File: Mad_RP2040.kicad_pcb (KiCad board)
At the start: 4 copper layers, 80 x 106.8 mm, 119 parts, among them J1 USB_C_Receptacle, Q1 2N7002PV,115, SW1 SW_SPST, SW10 SW_SPST, SW100 EVPAA202K, SW11 SW_SPST, SW12 SW_SPST, SW13 SW_SPST, SW14 SW_SPST, SW15 SW_SPST, SW16 SW_SPST, SW17 SW_SPST, SW18 SW_SPST, SW19 SW_SPST, SW2 SW_SPST, SW20 SW_SPST, SW3 SW_SPST, SW4 SW_SPST, SW5 SW_SPST, SW6 SW_SPST, SW7 SW_SPST, SW8 SW_SPST, SW9 SW_SPST, U2 ECMF02-2AMX6, U3 NCP1117-3.3, U4 W25Q128JVSIQ, U5 RP2040, X1 ECS-2520MVLC-120-CN

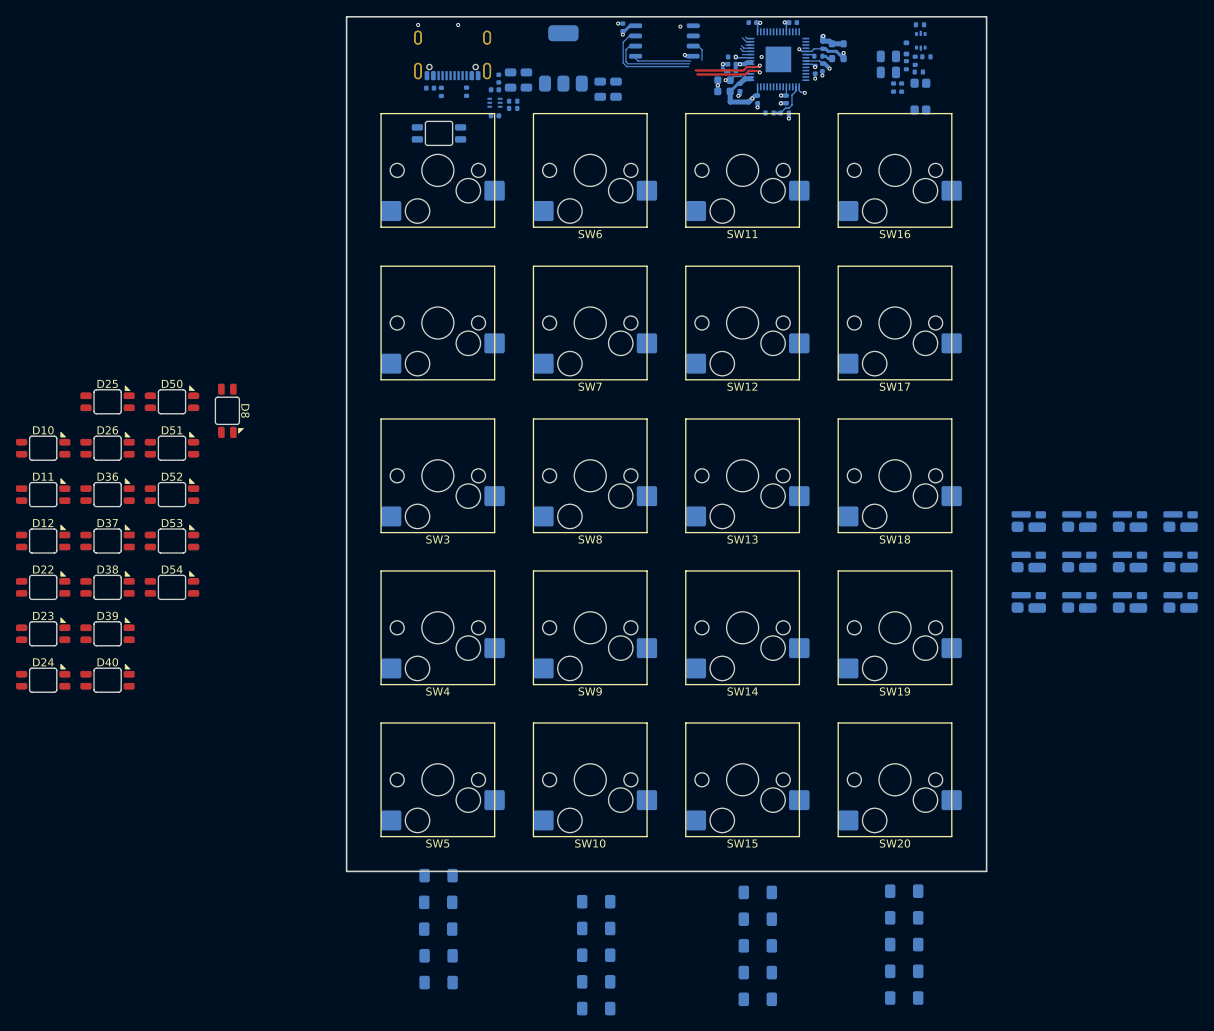
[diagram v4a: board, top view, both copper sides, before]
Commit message: Rough placement of components. Remove one layer of keys (4x4 -> 4x3)
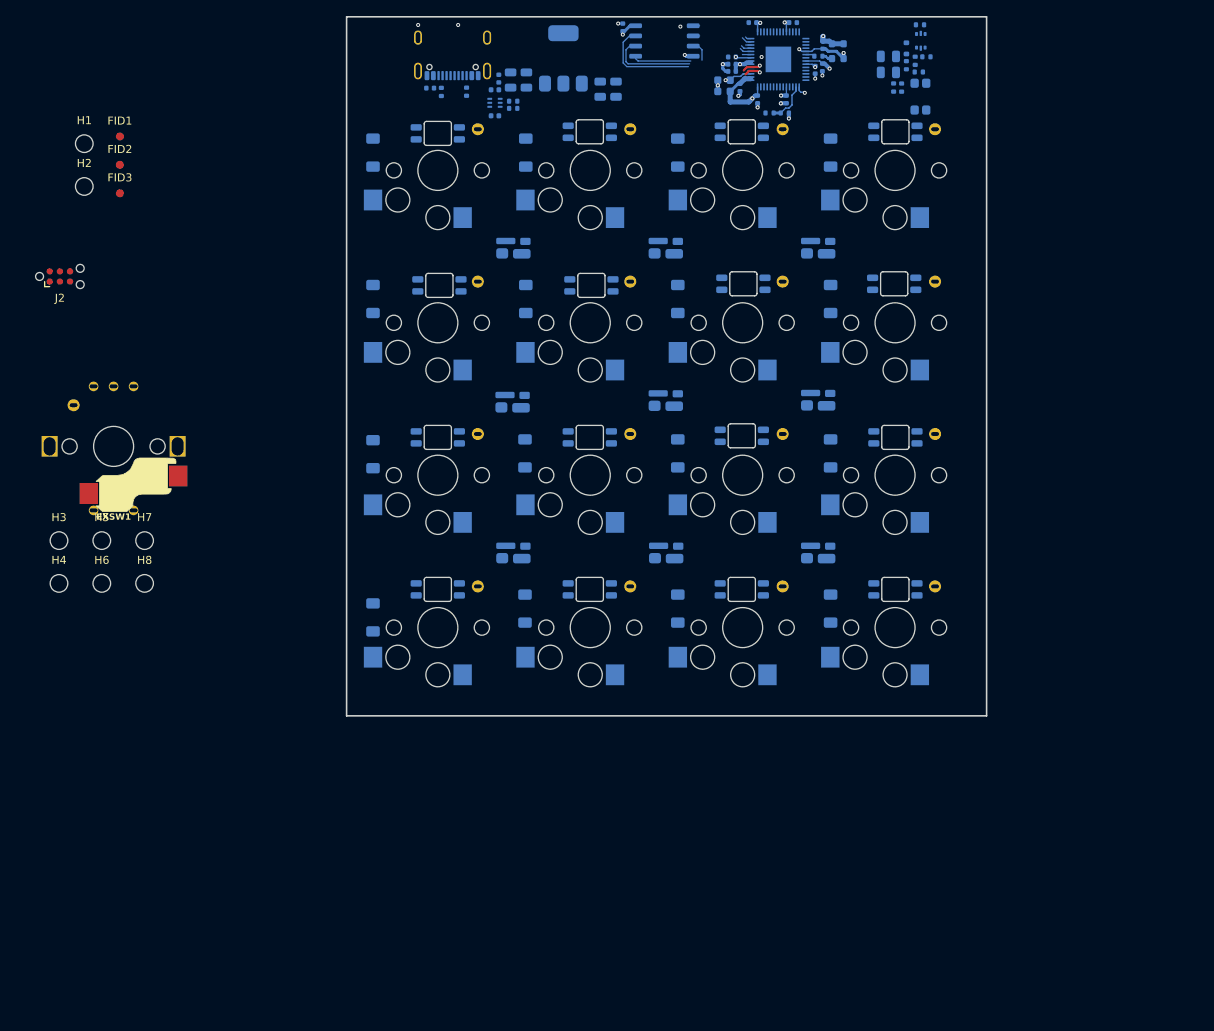
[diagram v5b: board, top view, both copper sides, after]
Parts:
- removed D12, D26, D40, D54: SK6812_MINI_E, Mad_Footprints:SK6812MINI-E
- removed D16, D30, D44: SK6812MINI, Mad_Footprints:SK6812MINI-012
- removed D21, D35, D49, D5: LL4148, Diode_SMD:D_MiniMELF
- removed SW10, SW15, SW20, SW5: SW_SPST, Mad_Footprints:SW_Hotswap_Kailh_MX_1.00u
- added EXSW1: RotaryEncoder_Switch, kbd:keyswitch_choc12_hotswap_1u_rotary_encoder_ec12, F.Cu at (91.4, 96.1)
- added FID1: Fiducial, Fiducial:Fiducial_1mm_Mask2mm, F.Cu at (92.2, 57.4)
- added FID2: Fiducial, Fiducial:Fiducial_1mm_Mask2mm, F.Cu at (92.2, 60.9)
- added FID3: Fiducial, Fiducial:Fiducial_1mm_Mask2mm, F.Cu at (92.2, 64.5)
- added H1: MountingHole_Pad, MountingHole:MountingHole_2.2mm_M2_DIN965, F.Cu at (87.8, 58.3)
- added H2: MountingHole_Pad, MountingHole:MountingHole_2.2mm_M2_DIN965, F.Cu at (87.8, 63.6)
- added H3: MountingHole_Pad, MountingHole:MountingHole_2.2mm_M2_DIN965, F.Cu at (84.6, 107.9)
- added H4: MountingHole_Pad, MountingHole:MountingHole_2.2mm_M2_DIN965, F.Cu at (84.6, 113.2)
- added H5: MountingHole_Pad, MountingHole:MountingHole_2.2mm_M2_DIN965, F.Cu at (90.0, 107.9)
- added H6: MountingHole_Pad, MountingHole:MountingHole_2.2mm_M2_DIN965, F.Cu at (90.0, 113.2)
- added H7: MountingHole_Pad, MountingHole:MountingHole_2.2mm_M2_DIN965, F.Cu at (95.3, 107.9)
- added H8: MountingHole_Pad, MountingHole:MountingHole_2.2mm_M2_DIN965, F.Cu at (95.3, 113.2)
- added J2: Conn_ARM_SWD_TagConnect_TC2030-NL, Connector:Tag-Connect_TC2030-IDC-NL_2x03_P1.27mm_Vertical, F.Cu at (84.7, 74.9)
- added T1: Tab, PCM_kikit:Tab, F.Cu at (84.3, 57.2)
- added T2: Tab, PCM_kikit:Tab, F.Cu at (84.3, 60.5)
- added T3: Tab, PCM_kikit:Tab, F.Cu at (84.3, 63.8)
- added T4: Tab, PCM_kikit:Tab, F.Cu at (84.3, 67.1)
- added U1: PCB, Mad_Footprints:BOM, F.Cu at (92.6, 68.0)
- D10, D11, D22, D23, D24, D25, D36, D37, D38, D39, D50, D51, D52, D53, D8: moved to B.Cu
- SW1, SW11, SW12, SW13, SW14, SW16, SW17, SW18, SW19, SW2, SW3, SW4, SW6, SW7, SW8, SW9: footprint Mad_Footprints:SW_Hotswap_Kailh_MX_1.00u -> kbd:keyswitch_choc12_hotswap_1u; moved to B.Cu
- moved D17 107.4 mm to (142.9, 59.4), turned to -90 degrees
- moved D31 106.3 mm to (161.9, 59.4), turned to -90 degrees
- moved D45 106.1 mm to (181.1, 59.4), turned to -90 degrees
- moved D1 104.1 mm to (123.8, 59.4), turned to -90 degrees
- moved D50 96.5 mm to (189.2, 56.8), turned to 180 degrees
- moved D51 92.6 mm to (189.0, 75.8), turned to 180 degrees
- moved D36 91.3 mm to (169.9, 56.8), turned to 180 degrees
- moved D52 90.7 mm to (189.2, 95.0), turned to 180 degrees
- moved D53 90.6 mm to (189.2, 114.0), turned to 180 degrees
- moved D22 88.9 mm to (150.9, 56.8), turned to 180 degrees
- moved D18 85.8 mm to (142.9, 77.7), turned to -90 degrees
- moved D37 85.7 mm to (170.2, 75.8), turned to 180 degrees
- moved D32 84.8 mm to (161.9, 77.7), turned to -90 degrees
- moved D46 84.5 mm to (181.1, 77.7), turned to -90 degrees
- moved D2 82.5 mm to (123.8, 77.7), turned to -90 degrees
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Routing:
- net /RP2040/RP2040/USB_D+: track 9.46 -> 3.46 mm
- net /RP2040/RP2040/USB_D-: track 9.25 -> 3.25 mm
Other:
- board size 80 x 106.8 mm -> 80 x 87.4 mm

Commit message: More placement, start routing, fix up some schematic connections
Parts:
- removed D14, D27, D28, D29, D42: SK6812MINI, Mad_Footprints:SK6812MINI-012
- removed H1, H3, H5, H7: MountingHole_Pad, MountingHole:MountingHole_2.2mm_M2_DIN965
- removed the SW1 at (132.0, 61.6)
- added C23: 100nF, Capacitor_SMD:C_0402_1005Metric, B.Cu at (138.1, 51.8)
- added D16: SK6812MINI, Mad_Footprints:SK6812MINI-012, B.Cu at (160.5, 90.2)
- added H10: MountingHole_Pad, MountingHole:MountingHole_2.2mm_M2_DIN965, F.Cu at (193.1, 46.4)
- added H11: MountingHole_Pad, MountingHole:MountingHole_2.2mm_M2_DIN965, F.Cu at (127.9, 46.4)
- H2, H4, H6, H8, J2: moved to B.Cu
- SW1: renamed from EXSW1; moved to B.Cu
- moved J2 115.9 mm to (196.9, 46.0), turned to -90 degrees
- moved H6 92.5 mm to (179.6, 90.2)
- moved H2 73.2 mm to (160.5, 71.1)
- moved H8 65.4 mm to (160.5, 109.2), turned to 180 degrees
- moved H4 61.4 mm to (141.5, 90.2)
- moved SW1 53.2 mm to (132.0, 61.6), turned to 180 degrees
- moved R9 9.51 mm to (180.4, 51.8), turned to 180 degrees
- moved R7 9.36 mm to (184.9, 49.3), turned to 90 degrees
- moved SW100 9.30 mm to (186.9, 44.8), turned to 180 degrees
- moved R15 8.63 mm to (180.4, 52.8), turned to 0 degrees
- moved C9 7.64 mm to (182.4, 52.3), turned to -90 degrees
- moved Q1 7.61 mm to (186.9, 50.8), turned to 180 degrees
- moved R6 5.00 mm to (188.9, 50.3), turned to -90 degrees
- moved C8 4.83 mm to (184.4, 52.3), turned to -90 degrees
- moved R8 4.74 mm to (185.9, 47.3), turned to 0 degrees
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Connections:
- D22 pad 2: +5V -> Net-(D22-DOUT)
- D25 pad 4: Net-(D25-DIN) -> Net-(D11-DOUT)
- D36 pad 4: +5V -> Net-(D22-DOUT)
- D41 pad 1: Net-(D27-DOUT) -> Net-(D13-DOUT)
- D43 pad 1: Net-(D29-DOUT) -> Net-(D15-DOUT)
- D43 pad 3: Net-(D16-DIN) (its old number) -> unconnected-(D43-DOUT-Pad3)
- D53 pad 4: Net-(D53-DIN) -> Net-(D39-DOUT)
- SW1 pad A: /RE0A -> /REB
- SW1 pad B: /REB -> /RE0A
- SW1 pad S1: GND -> Net-(D1-A)
- SW1 pad S2: /KEYEX1 -> /Col0
- U5 pad 12: /RP2040/IO_9 -> /Col0
- U5 pad 13: /RP2040/IO_10 -> /Col1
- U5 pad 14: /RP2040/ENC1A -> /Col2
- U5 pad 15: /RP2040/ENC1B -> /Col3
- U5 pad 16: /RP2040/ENC2A -> /RP2040/ENC1A
- U5 pad 17: /RP2040/ENC2B -> /RP2040/ENC1B
- U5 pad 18: /RP2040/ENC3A -> /RP2040/ENC2A
- U5 pad 27: /RP2040/ENC3B -> /RP2040/ENC2B
- U5 pad 8: /RP2040/IO_6 -> /Row2
- U5 pad 9: /Col0 -> /Row3
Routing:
- net +5V: track 0.00 -> 288.6 mm, vias 0 -> 16
- net /Col0: track 0.00 -> 97.2 mm
- net /Col1: track 0.00 -> 96.6 mm
- net /Col2: track 0.00 -> 90.5 mm
- net Net-(D13-DIN): track 0.00 -> 74.5 mm, vias 0 -> 2
- net /Col3: track 0.00 -> 66.7 mm
- net Net-(D16-DIN): track 0.00 -> 47.2 mm, vias 0 -> 2
- net Net-(D15-DIN): track 0.00 -> 46.9 mm, vias 0 -> 2
- net /RP2040/RP2040/QSPI_~{CS}: track 1.54 -> 41.7 mm, vias 0 -> 2
- net GND: track 16.1 -> 52.9 mm, vias 14 -> 93
- net Net-(D15-DOUT): track 0.00 -> 36.6 mm, vias 0 -> 2
- net Net-(D13-DOUT): track 0.00 -> 36.5 mm, vias 0 -> 2
- net Net-(D10-DOUT): track 0.00 -> 31.6 mm
- net /RP2040/RP2040/USB_D-: track 3.25 -> 32.2 mm, vias 1 -> 2
- net /RP2040/RP2040/USB_D+: track 3.46 -> 32.2 mm, vias 1 -> 2
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- added copper zone on B.Cu, net +5V
- added copper zone on B.Cu, net /PreFIlterGND
- added copper zone on In1.Cu, net /PreFIlterGND
- added copper zone on In2.Cu, net /PreFIlterGND
- added copper zone on In1.Cu, net /RP2040/3V3
- added copper zone on B.Cu, net GND
- added copper zone on F.Cu, net GND
- added copper zone on In1.Cu, net GND
- added copper zone on In2.Cu, net GND
- added copper zone on B.Cu, net VBUS
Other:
- board size 80 x 87.4 mm -> 77.2 x 86.4 mm

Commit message: Update tabs
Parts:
- removed FID1, FID2, FID3: Fiducial, Fiducial:Fiducial_1mm_Mask2mm
- removed U1: PCB, Mad_Footprints:BOM
- moved T1 119.5 mm to (199.2, 90.3), turned to 180 degrees
- moved T4 98.1 mm to (160.4, 129.0), turned to 90 degrees
- moved T2 73.0 mm to (154.9, 42.0), turned to -90 degrees
- moved T3 45.6 mm to (121.4, 90.3)

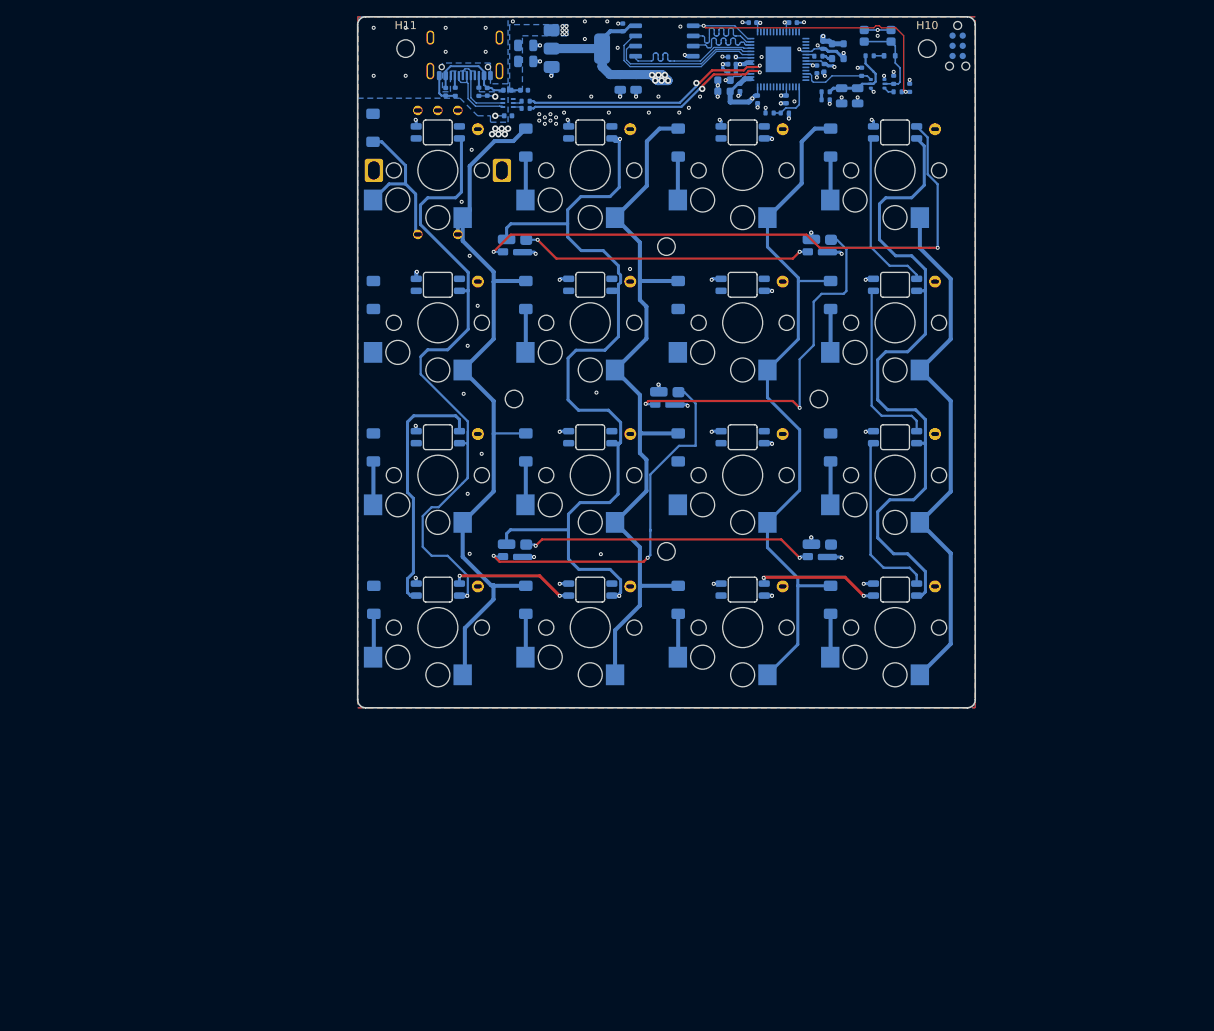
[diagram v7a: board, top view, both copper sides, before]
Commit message: Review Schematic, Add TRS connector. Continue routing
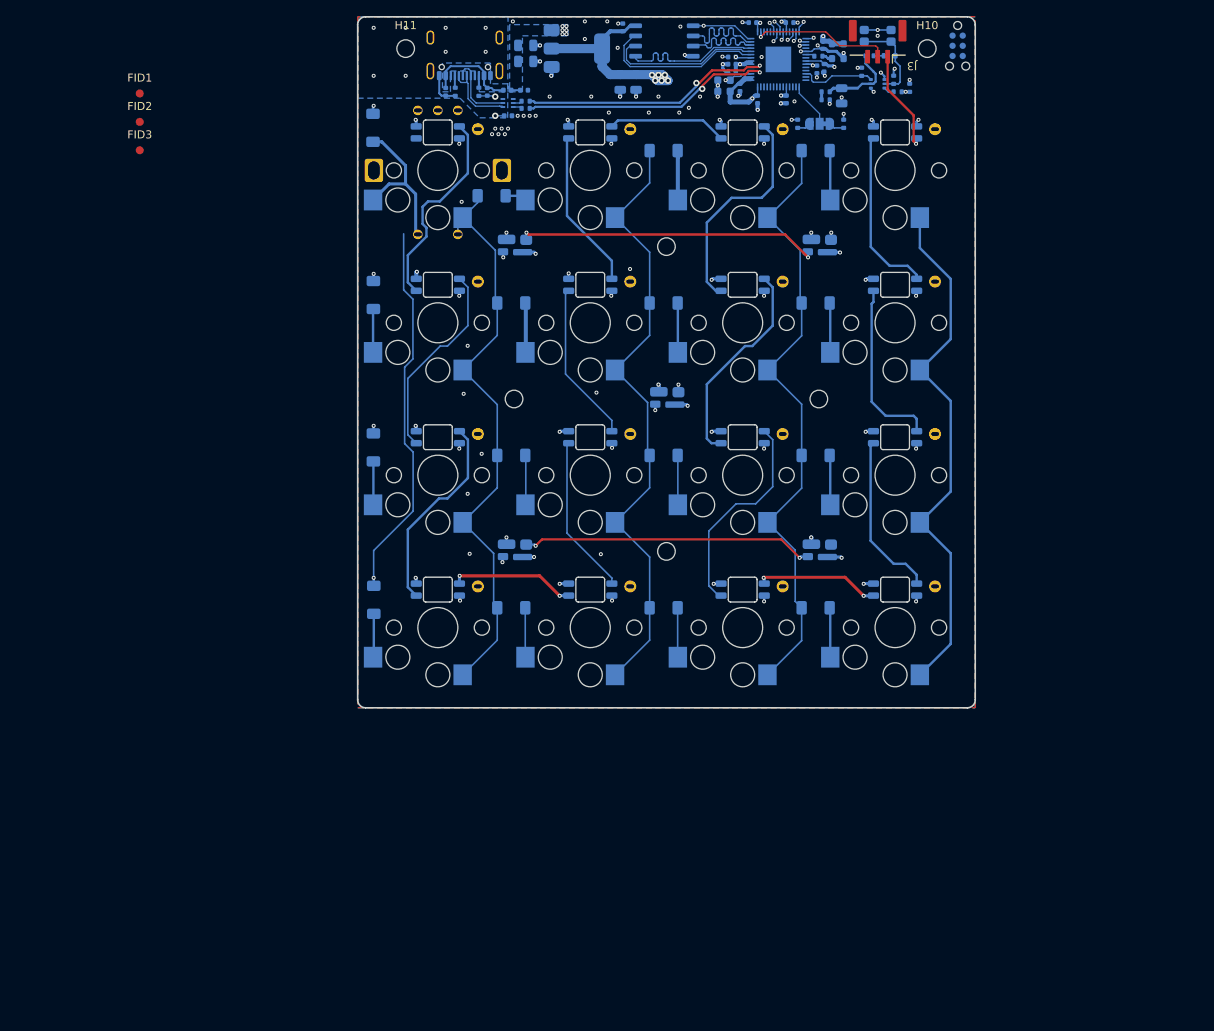
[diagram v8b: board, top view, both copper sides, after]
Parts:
- removed C8: 10uF, Capacitor_SMD:C_0805_2012Metric
- added FID1: Fiducial, Fiducial:Fiducial_1mm_Mask2mm, F.Cu at (94.7, 52.0)
- added FID2: Fiducial, Fiducial:Fiducial_1mm_Mask2mm, F.Cu at (94.7, 55.5)
- added FID3: Fiducial, Fiducial:Fiducial_1mm_Mask2mm, F.Cu at (94.7, 59.1)
- added J3: TRS, Mad_Footprints:SM03B-GHS, F.Cu at (186.9, 47.4)
- added JP1: Split Hand Detect Selector, Jumper:SolderJumper-3_P1.3mm_Bridged12_RoundedPad1.0x1.5mm, B.Cu at (179.7, 55.8)
- added U1: PCB, Mad_Footprints:BOM, F.Cu at (98.6, 52.0)
- moved R3 9.36 mm to (182.7, 55.8), turned to -90 degrees
- moved D17 7.90 mm to (138.7, 64.8), turned to 0 degrees
- moved D45 2.12 mm to (179.2, 59.1), turned to 0 degrees
- moved D46 2.12 mm to (179.2, 78.2), turned to 0 degrees
- moved D47 2.12 mm to (179.2, 97.2), turned to 0 degrees
- moved D48 2.12 mm to (179.2, 116.3), turned to 0 degrees
- moved R4 2.10 mm to (176.9, 55.8), turned to 90 degrees
- moved D18 2.07 mm to (141.1, 78.2), turned to 0 degrees
- moved D19 2.07 mm to (141.1, 97.2), turned to 0 degrees
- moved D20 2.07 mm to (141.1, 116.3), turned to 0 degrees
- moved D31 2.07 mm to (160.2, 59.1), turned to 0 degrees
- moved D32 2.07 mm to (160.2, 78.2), turned to 0 degrees
- moved D33 2.07 mm to (160.2, 97.2), turned to 0 degrees
- moved D34 2.07 mm to (160.2, 116.3), turned to 0 degrees
- moved C17 0.42 mm to (175.9, 43.1)
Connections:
- net /RP2040/RX0 renamed /LED
- net /RP2040/SCL1 renamed /RP2040/SCL
- net /RP2040/SDA1 renamed /RP2040/SDA
- R3 pad 2: /RP2040/RP2040/GPIO18 -> Net-(JP1-A)
- R4 pad 1: /RP2040/RP2040/GPIO18 -> Net-(JP1-B)
- SW1 pad A: /REB -> /REA
- SW1 pad B: /RE0A -> /REB
- U5 pad 16: /RP2040/ENC1A -> /REA
- U5 pad 17: /RP2040/ENC1B -> /REB
- U5 pad 2: /TX0 -> /TX
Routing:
- net +5V: track 288.6 -> 28.7 mm, vias 16 -> 27
- net Net-(D13-DIN): track 74.5 -> 1.63 mm
- net /Row3: track 0.00 -> 48.5 mm, vias 0 -> 2
- net Net-(D36-DOUT): track 0.00 -> 27.7 mm
- net Net-(D38-DOUT): track 0.00 -> 26.5 mm
- net Net-(D37-DOUT): track 0.00 -> 26.4 mm
- net Net-(D6-DOUT): track 0.00 -> 25.8 mm
- net Net-(D10-DIN): track 0.00 -> 25.1 mm
- net /Col0: track 97.2 -> 75.1 mm, vias 0 -> 1
- net Net-(D23-DIN): track 0.00 -> 20.1 mm
- net Net-(D22-DIN): track 0.00 -> 20.0 mm
- net Net-(D24-DIN): track 0.00 -> 20.0 mm
- net /TX: track 0.00 -> 18.1 mm, vias 0 -> 1
- net /Col1: track 96.6 -> 79.3 mm, vias 0 -> 1
- net Net-(D22-DOUT): track 0.00 -> 14.9 mm
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- added copper zone on In1.Cu, net +5V
